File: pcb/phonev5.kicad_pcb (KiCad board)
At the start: 4 copper layers, 81 x 115.8 mm, 40 parts, among them J1 coin, J2 keypad, J3 display, J4 RJ9, J5 mic, J6 card_reader, J7 speaker, Q1 IRF9540N, U2 TDA2822M

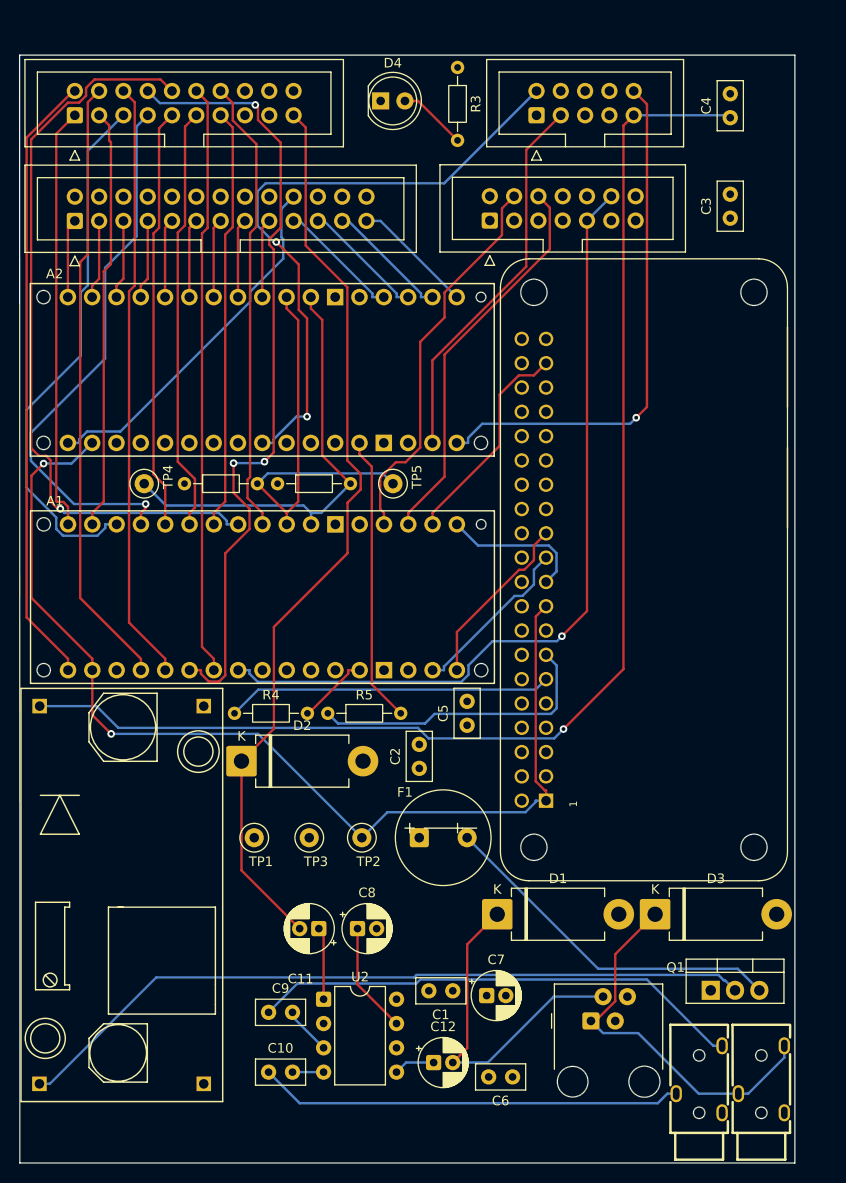
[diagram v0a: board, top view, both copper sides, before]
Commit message: Arduino: GPIO reset flashing, remove CMD_FLASH_MODE hack; add CLAUDE.md
Replace the old deploy_display.sh (uhubctl power-cycling, 200-attempt
race loop, CMD_FLASH_MODE silent mode) with a clean GPIO-reset approach
now that the Pi has direct RST connections to both Arduinos:
- GPIO17/GEN0 (pin 11) → Arduino Alpha RST
- GPIO27/GEN2 (pin 13) → Arduino Beta RST (required bodge wire; trace
  missing from phonev5 PCB — documented in pcb/README.md errata)

Changes:
- deploy_display.sh: assert GPIO27 reset (open-drain), wait for device
  to cycle, flash with avrdude; remove uhubctl/1200-baud/race loop
- deploy_keypad.sh: new script, same approach via GPIO17
- Makefile: replace flash_display with deploy_display/deploy_keypad/deploy
- display.ino: remove CMD_FLASH_MODE (0xFF) and silentUntil hack
- pcb/README.md: add Known PCB Errata section for missing Reset 2 trace
- CLAUDE.md: initial project guidance for Claude Code

Co-Authored-By: Claude Sonnet 4.6 <noreply@anthropic.com>
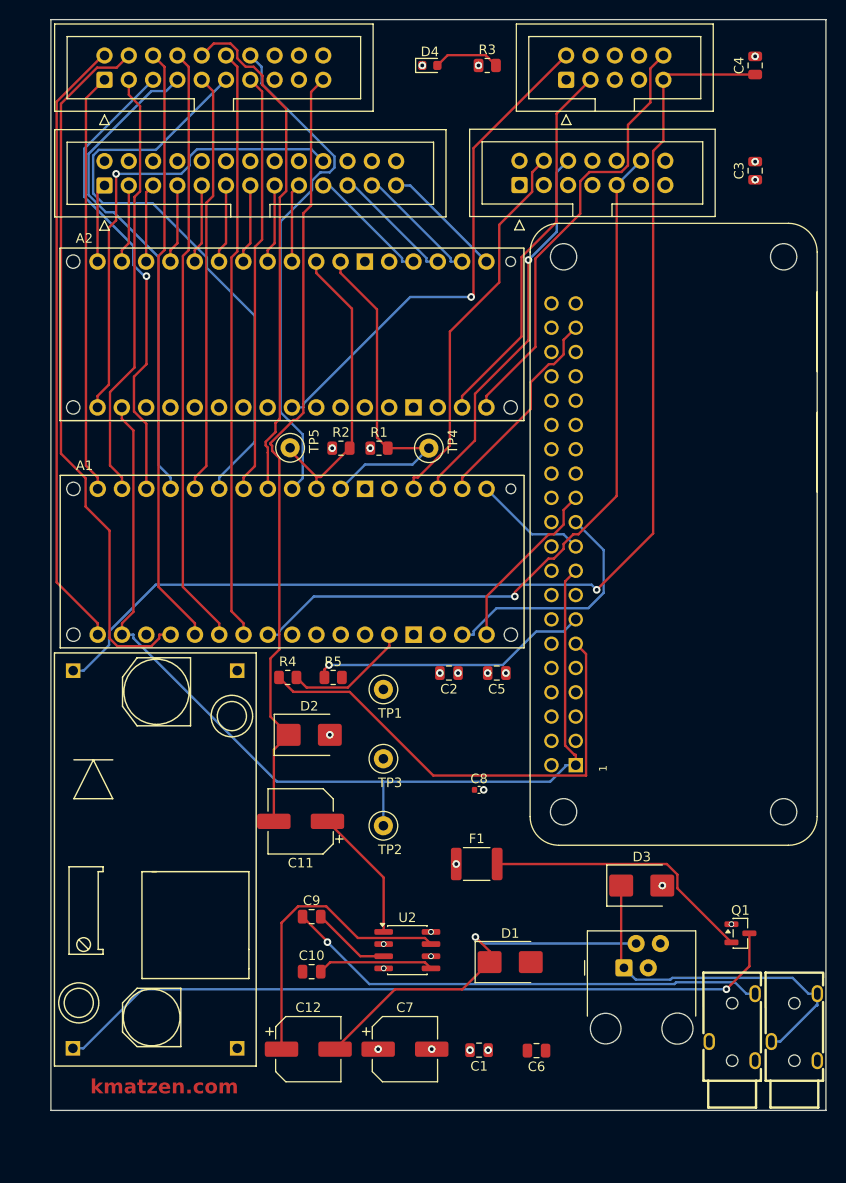
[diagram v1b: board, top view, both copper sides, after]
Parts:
- C1, C10, C2, C3, C4, C5, C6, C9: footprint Capacitor_THT:C_Disc_D5.0mm_W2.5mm_P2.50mm -> Capacitor_SMD:C_0805_2012Metric
- C11, C12, C7: footprint Capacitor_THT:CP_Radial_D5.0mm_P2.00mm -> Capacitor_SMD:CP_Elec_6.3x5.4
- C8: footprint Capacitor_THT:CP_Radial_D5.0mm_P2.00mm -> Capacitor_SMD:C_0402_1005Metric
- D1, D2, D3: footprint Diode_THT:D_DO-201AD_P12.70mm_Horizontal -> Diode_SMD:D_SMB
- D4: value Green LED -> Red LED; footprint LED_THT:LED_D5.0mm -> LED_SMD:LED_0603_1608Metric
- F1: footprint footprints:Fuse_Radial_D10.0mm_P5.00mm -> Fuse:Fuse_1812_4532Metric
- Q1: value IRF9540N -> AO3401A; footprint footprints:TO-220-3_Vertical_GSD -> Package_TO_SOT_SMD:SOT-23
- R1, R2, R3, R4, R5: footprint Resistor_THT:R_Axial_DIN0204_L3.6mm_D1.6mm_P7.62mm_Horizontal -> Resistor_SMD:R_0805_2012Metric
- U2: value TDA2822M -> PT2308-S; footprint Package_DIP:DIP-8_W7.62mm -> Package_SO:SOIC-8_3.9x4.9mm_P1.27mm
- moved TP4 30.0 mm to (79.5, 84.8)
- moved TP1 20.6 mm to (74.8, 110.0)
- moved C8 19.3 mm to (84.8, 120.5)
- moved R2 16.8 mm to (70.3, 84.8)
- moved C12 13.2 mm to (66.9, 147.6)
- moved C10 11.4 mm to (67.2, 139.5)
- moved TP5 11.4 mm to (65.0, 84.8)
- moved C11 11.4 mm to (66.1, 123.8)
- moved TP3 11.3 mm to (74.8, 117.2)
- moved R1 11.2 mm to (74.3, 84.8)
- moved C9 11.0 mm to (67.2, 133.8)
- moved C2 10.4 mm to (81.6, 108.3), turned to 180 degrees
- moved C7 10.2 mm to (77.0, 147.6)
- moved U2 10.1 mm to (77.2, 137.2)
- moved D2 7.60 mm to (67.0, 114.8)
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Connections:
- U2 pad 4: Net-(U2-IN_B) -> GND
- U2 pad 5: Net-(U2-OUT_B) -> Net-(U2-IN_B)
- U2 pad 6: 5V_MAIN -> GND
- U2 pad 7: Net-(U2-RIPPLE) -> Net-(U2-OUT_B)
- U2 pad 8: unconnected-(U2-NC-Pad8) -> 5V_MAIN
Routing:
- net speaker_receiver_pre+: track 44.4 -> 0.00 mm
- net RESET2: track 30.0 -> 0.00 mm
- net Net-(U2-OUT_B): track 4.29 -> 31.2 mm
- net key_hook_up: track 78.2 -> 53.9 mm, vias 1 -> 0
- net key_col_7: track 83.5 -> 62.8 mm, vias 3 -> 0
- net key_row_3: track 44.5 -> 63.6 mm
- net PI_RESET1: track 34.0 -> 50.6 mm
- net speaker_front+: track 95.6 -> 82.1 mm
- net scl: track 44.1 -> 31.3 mm
- net coin_tx: track 65.4 -> 53.1 mm, vias 2 -> 1
- net Net-(U2-RIPPLE): track 11.6 -> 0.00 mm
- net key_col_5: track 64.0 -> 74.6 mm
- net disp_x6: track 38.4 -> 49.0 mm, vias 0 -> 1
- net sda: track 46.5 -> 36.8 mm
- net coin_reset: track 55.3 -> 46.4 mm, vias 1 -> 0
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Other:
- board size 81 x 115.8 mm -> 81 x 114 mm
- board text added: "kmatzen.com"
